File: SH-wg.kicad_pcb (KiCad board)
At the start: 4 copper layers, 55.6 x 79.2 mm, 68 parts, among them J101 Aux PCB Conn Male, J102 Aux PCB Conn Female, J201 Conn_01x05, J501 Conn_01x04, J701 Conn_02x03_Odd_Even, U201 SN65HVD231, U301 ESP32-WROOM-32E, U601 XL1509-3.3, U801 AH1902

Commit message: Add headers & LEDs
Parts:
- added D803: GREEN LED, LED_SMD:LED_0603_1608Metric, F.Cu at (92.2, 97.8)
- added D804: GREEN LED, LED_SMD:LED_0603_1608Metric, F.Cu at (102.8, 97.8)
- added J301: JTAG, Connector_IDC:IDC-Header_2x05_P2.54mm_Vertical, F.Cu at (99.8, 88.6)
- added J302: Digital IO, Connector_PinHeader_2.54mm:PinHeader_1x05_P2.54mm_Vertical, F.Cu at (94.7, 62.0)
- added J303: Analog IO, Connector_PinHeader_2.54mm:PinHeader_1x05_P2.54mm_Vertical, F.Cu at (64.3, 88.6)
- added J401: Power, Connector_PinHeader_2.54mm:PinHeader_2x03_P2.54mm_Vertical, F.Cu at (79.5, 88.6)
- added Q801: 2N7002, Package_TO_SOT_SMD:SOT-23, F.Cu at (62.2, 64.8)
- added R803: 2.2k, Resistor_SMD:R_0402_1005Metric, F.Cu at (92.8, 96.2)
- added R804: 2.2k, Resistor_SMD:R_0402_1005Metric, F.Cu at (102.2, 96.2)
- added R805: 10k, Resistor_SMD:R_0402_1005Metric, F.Cu at (65.5, 65.8)
- moved D802 40.9 mm to (96.2, 58.5)
- moved R802 38.9 mm to (93.5, 58.2), turned to 0 degrees
- moved U801 7.08 mm to (80.5, 97.5)
- moved C801 7.08 mm to (82.5, 97.8)
- moved D805 0.95 mm to (61.1, 61.1)
- moved R806 0.95 mm to (62.8, 60.8)
- renumbered D803 to D805, R803 to R806
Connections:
- D805 pad 1: GND -> Net-(D805-Pad1)
- J101 pad 10: /CAN_TX -> /RXD
- J101 pad 3: /EN -> /IO0
- J101 pad 4: /SCL -> /CAN_TX
- J101 pad 5: /IO0 -> /EN
- J101 pad 6: /SDA -> /CAN_RX
- J101 pad 7: /TXD -> /SCL
- J101 pad 8: /CAN_RX -> /TXD
- J101 pad 9: /RXD -> /SDA
- U301 pad 10: /ESP32/IO25 -> /CAN_RX
- U301 pad 11: /ESP32/IO26 -> /CAN_TX
- U301 pad 12: /ESP32/IO27 -> /CAN_LED_EN
- U301 pad 13: /ESP32/IO14 -> /ESP32/TMS
- U301 pad 14: /ESP32/IO12 -> /ESP32/TDI
- U301 pad 16: /ESP32/IO13 -> /ESP32/TCK
- U301 pad 23: /ESP32/IO15 -> /ESP32/TDO
- U301 pad 29: /ESP32/IO5 -> /RED_LED
- U301 pad 6: /CAN_RX -> /ESP32/IO34
- U301 pad 7: /CAN_TX -> /ESP32/IO35

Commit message: Finish 0.1.0 design
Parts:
- removed C411, C412, C413, C414, C415, C416, C417, C418, C419, C420: 100nF, Capacitor_SMD:C_0402_1005Metric
- added G401: Hat Labs pictogram, SH-wg:HL_pictogram_6.3mm, F.Cu at (70.0, 80.9)
- added G402: Hat Labs logo, SH-wg:Hat_Labs_20mm, B.Cu at (91.1, 129.4)
- added G403: Hat Labs logo large, SH-wg:Hat_Labs_25.4mm, B.Cu at (79.5, 67.1)
- added G404: WEEE logo, Symbol:WEEE-Logo_5.6x8mm_SilkScreen, B.Cu at (79.7, 81.5)
- added G405: OSHW logo, Symbol:OSHW-Logo2_9.8x8mm_SilkScreen, B.Cu at (88.3, 80.8)
- H401: footprint SH-ESP32:MountingSlot_3.2mm_M3_Unplated -> MountingHole:MountingHole_3.2mm_M3
- J302: footprint Connector_PinHeader_2.54mm:PinHeader_1x05_P2.54mm_Vertical -> Connector_PinHeader_2.54mm:PinHeader_1x04_P2.54mm_Vertical
- L602: footprint SH-ESP32:SMMS0650-1R0M -> SH-wg:SMMS0650-1R0M
- R802: value 2k -> 1.5k
- R803, R804: value 2.2k -> 2k
- R806: value 2k -> 2.2k
- U301: footprint SH-ESP32:ESP32-WROOM-32-HandSolder -> SH-wg:ESP32-WROOM-32-HandSolder
- moved C404 63.5 mm to (108.1, 62.1), turned to 90 degrees
- moved C408 60.5 mm to (106.5, 88.0), turned to 0 degrees
- moved C403 57.5 mm to (97.1, 66.6), turned to 0 degrees
- moved C406 53.7 mm to (97.5, 96.2)
- moved C705 52.6 mm to (103.1, 133.8), turned to 90 degrees
- moved C405 51.2 mm to (88.2, 96.2), turned to 0 degrees
- moved C703 49.0 mm to (102.4, 116.5), turned to -90 degrees
- moved C402 45.5 mm to (97.1, 80.6), turned to 180 degrees
- moved C704 45.5 mm to (96.5, 121.6)
- moved C410 25.3 mm to (63.1, 83.8), turned to 180 degrees
- moved C401 24.3 mm to (67.7, 68.8), turned to 0 degrees
- moved C409 24.1 mm to (66.3, 61.8), turned to 90 degrees
- moved C707 21.6 mm to (75.9, 122.5)
- moved C701 20.2 mm to (70.8, 131.3), turned to -90 degrees
- moved C407 19.8 mm to (68.0, 74.2)
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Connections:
- J302 pad 1: /ESP32/IO18 -> /ESP32/IO19
- J302 pad 2: /ESP32/IO19 -> /ESP32/IO21
- J302 pad 3: /ESP32/IO21 -> /ESP32/IO22
- J302 pad 4: /ESP32/IO22 -> /ESP32/IO23
- U301 pad 30: /ESP32/IO18 -> /HALL
- U301 pad 34: /TXD -> /RXD
- U301 pad 35: /RXD -> /TXD
- U801 pad 5: /HALL_OUTPUT -> /HALL
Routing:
- net /CAN_TX: track 0.00 -> 75.4 mm, vias 0 -> 5
- net /CAN_RX: track 0.00 -> 63.6 mm, vias 0 -> 8
- net /CAN_LED_EN: track 0.00 -> 54.5 mm, vias 0 -> 5
- net /SCL: track 0.00 -> 46.8 mm, vias 0 -> 3
- net /ESP32/TMS: track 0.00 -> 44.2 mm, vias 0 -> 2
- net /SDA: track 0.00 -> 44.1 mm, vias 0 -> 3
- net /TXD: track 0.00 -> 40.6 mm, vias 0 -> 2
- net /YELLOW_LED: track 0.00 -> 37.5 mm, vias 0 -> 4
- net /HALL: track 0.00 -> 36.3 mm, vias 0 -> 4
- net /ESP32/TDI: track 0.00 -> 35.7 mm, vias 0 -> 2
- net /ESP32/SENSOR_VP: track 0.00 -> 34.8 mm, vias 0 -> 3
- net /ESP32/TCK: track 0.00 -> 33.6 mm, vias 0 -> 2
- net /ESP32/IO34: track 0.00 -> 33.0 mm, vias 0 -> 3
- net /RXD: track 0.00 -> 31.6 mm, vias 0 -> 2
- net /ESP32/IO32: track 0.00 -> 31.2 mm, vias 0 -> 3
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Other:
- board size 55.6 x 79.2 mm -> 54.6 x 79.2 mm
- board text added: "19"
- board text added: "21"
- board text added: "22"
- board text added: "23"
- board text added: "32"
- board text added: "33"
- board text added: "34"
- board text added: "3V3"
- board text added: "GND"
- board text added: "I2C"
- board text added: "JTAG"
- board text added: "Prog"
- board text added: "SCL"
- board text added: "SDA"
- board text added: "Sailor Hat WiFi Gateway"
- board text added: "VN"
- board text added: "VP"
- board text added: "v0.1.0"
- board text removed: "SH-ESP32"
- board text removed: "Sailor Hat with ESP32"
- board text removed: "https://github.com/hatlabs/SH-ESP32-hardware/"

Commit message: Prepare final 0.1.0 proto
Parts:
- added REF**: Tab, kikit:Tab, F.Cu at (80.8, 83.8)
- added REF**: Tab, kikit:Tab, F.Cu at (42.8, 127.5)
- added REF**: Tab, kikit:Tab, F.Cu at (97.2, 127.6)
- added REF**: Tab, kikit:Tab, F.Cu at (96.5, 44.8)
- added REF**: Tab, kikit:Tab, F.Cu at (70.0, 138.8)
- added REF**: Tab, kikit:Tab, F.Cu at (77.3, 39.1)
- added REF**: Tab, kikit:Tab, F.Cu at (42.2, 57.6)
- added REF**: Tab, kikit:Tab, F.Cu at (70.0, 116.3)
- added REF**: Tab, kikit:Tab, F.Cu at (96.5, 70.5)
- D603: value SS24FL -> DSS34
- L601: value NLCV32T-100K-PFR -> CBC3225T100KR
- U201: value SN65HVD231 -> SN65HVD232DR
- moved C405 24.1 mm to (71.5, 78.8)
- moved C406 24.1 mm to (80.8, 78.8)
- moved R801 24.1 mm to (93.5, 69.5)
- moved U801 24.1 mm to (63.8, 80.1)
- moved C302 24.1 mm to (51.3, 41.7)
- moved C407 24.1 mm to (51.3, 56.8)
- moved D802 24.1 mm to (79.5, 41.1)
- moved G401 24.1 mm to (53.3, 63.5)
- moved H404 24.1 mm to (80.3, 57.6)
- moved J302 24.1 mm to (78.0, 44.6)
- moved Q801 24.1 mm to (45.5, 47.4)
- moved R802 24.1 mm to (76.8, 40.9)
- moved R805 24.1 mm to (48.8, 48.4)
- moved U301 24.1 mm to (63.3, 49.0)
- moved C401 24.1 mm to (51.0, 51.4)
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- renumbered H401 to H404
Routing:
- net GND: vias 78 -> 76
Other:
- board size 54.6 x 79.2 mm -> 54.6 x 99.2 mm
- board text removed: "JLCJLCJLCJLC"

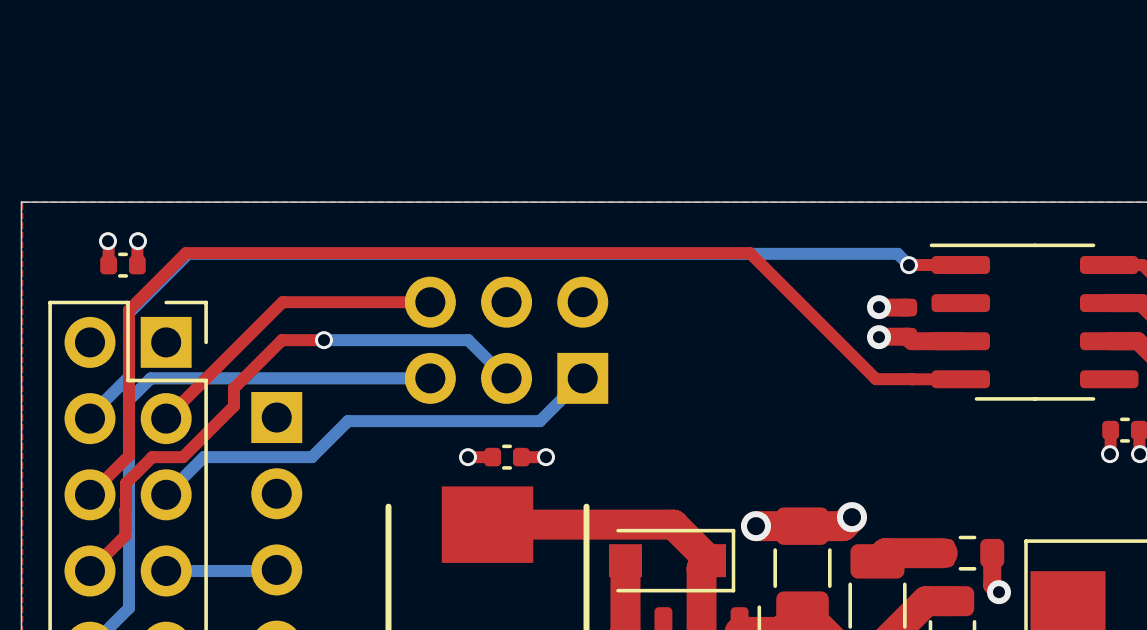
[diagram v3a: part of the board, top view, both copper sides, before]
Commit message: Add a pull-up resistor to CAN TX line
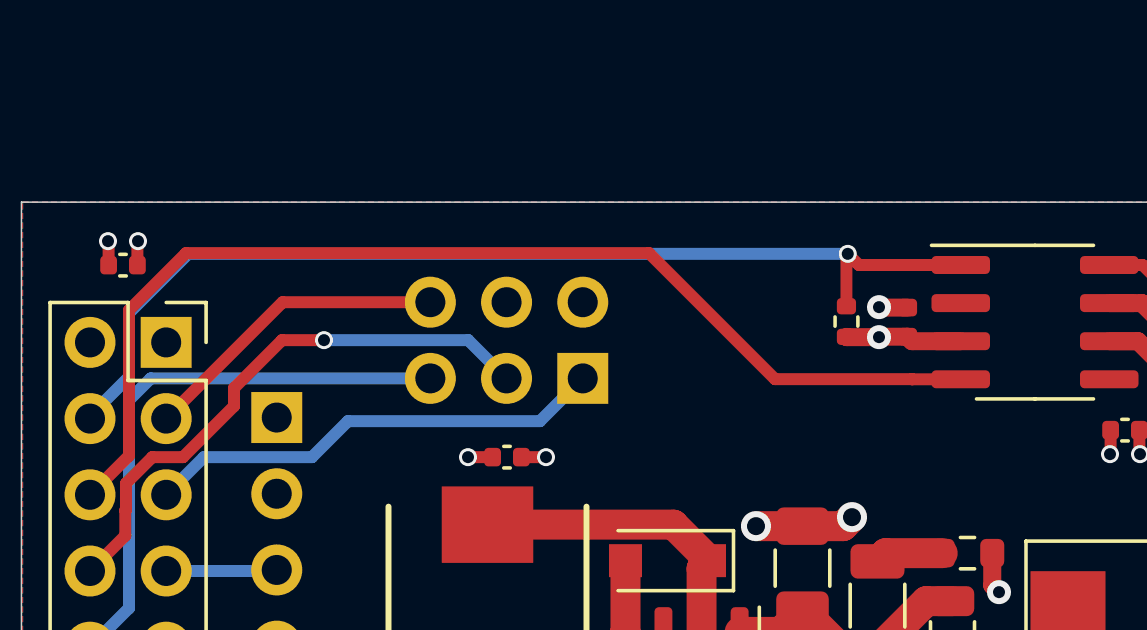
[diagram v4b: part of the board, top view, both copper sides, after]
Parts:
- added R202: 10k, Resistor_SMD:R_0402_1005Metric, F.Cu at (70.5, 120.6)
- D603: value DSS34 -> B5819W
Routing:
- net /CAN_TX_1: track 32.8 -> 34.5 mm
- net +3V3_1: track 20.8 -> 21.9 mm
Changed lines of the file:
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@@
     (descr "D_SOD-123F")
     (tags "D_SOD-123F")
-    (property "LCSC" "C511866")
+    (property "LCSC" "C8598")
     (property "Notes" "")
     (property "Sheetfile" "power-input.kicad_sch")
@@
       (effects (font (size 1 1) (thickness 0.15)))
     )
-    (fp_text value "DSS34" (at 0 2.1) (layer "F.Fab") hide
+    (fp_text value "B5819W" (at 0 2.1) (layer "F.Fab") hide
       (effects (font (size 1 1) (thickness 0.15)))
     )
@@
     (pad "" np_thru_hole circle (at 0 0) (size 3.2 3.2) (drill 3.2) (layers *.Cu *.Mask))
   )
+  (footprint "Resistor_SMD:R_0402_1005Metric" (layer "F.Cu")
+    (at 70.5 120.6 90)
+    (descr "Resistor SMD 0402 (1005 Metric), square (rectangular) end terminal, IPC_7351 nominal, (Body size source: IPC-SM-782 page 72, https://www.pcb-3d.com/wordpress/wp-content/uploads/ipc-sm-782a_amendment_1_and_2.pdf), generated with kicad-footprint-generator")
+    (tags "resistor")
+    (property "LCSC" "C25744")
+    (property "Sheetfile" "canbus.kicad_sch")
+    (property "Sheetname" "CAN bus")
+    (attr smd)
+    (fp_text reference "R202" (at 0 -1.17 90) (layer "F.SilkS") hide
+      (effects (font (size 1 1) (thickness 0.15)))
+    )
+    (fp_text value "10k" (at 0 1.17 90) (layer "F.Fab") hide
+      (effects (font (size 1 1) (thickness 0.15)))
+    )
+    (fp_text user "${REFERENCE}" (at 0 0 90) (layer "F.Fab") hide
+      (effects (font (size 0.26 0.26) (thickness 0.04)))
+    )
+    (fp_line (start -0.153641 0.38) (end 0.153641 0.38) (layer "F.SilkS") (width 0.12))
+    (fp_line (start -0.153641 -0.38) (end 0.153641 -0.38) (layer "F.SilkS") (width 0.12))
+    (fp_line (start 0.93 -0.47) (end 0.93 0.47) (layer "F.CrtYd") (width 0.05))
+    (fp_line (start -0.93 0.47) (end -0.93 -0.47) (layer "F.CrtYd") (width 0.05))
+    (fp_line (start 0.93 0.47) (end -0.93 0.47) (layer "F.CrtYd") (width 0.05))
+    (fp_line (start -0.93 -0.47) (end 0.93 -0.47) (layer "F.CrtYd") (width 0.05))
+    (fp_line (start -0.525 0.27) (end -0.525 -0.27) (layer "F.Fab") (width 0.1))
+    (fp_line (start 0.525 0.27) (end -0.525 0.27) (layer "F.Fab") (width 0.1))
+    (fp_line (start 0.525 -0.27) (end 0.525 0.27) (layer "F.Fab") (width 0.1))
+    (fp_line (start -0.525 -0.27) (end 0.525 -0.27) (layer "F.Fab") (width 0.1))
+    (pad "1" smd roundrect (at -0.51 0 90) (size 0.54 0.64) (layers "F.Cu" "F.Paste" "F.Mask") (roundrect_rratio 0.25)
+      (net 54 "+3V3_1") (pintype "passive"))
+    (pad "2" smd roundrect (at 0.51 0 90) (size 0.54 0.64) (layers "F.Cu" "F.Paste" "F.Mask") (roundrect_rratio 0.25)
+      (net 50 "/CAN_TX_1") (pintype "passive"))
+    (model "${KICAD6_3DMODEL_DIR}/Resistor_SMD.3dshapes/R_0402_1005Metric.wrl"
+      (offset (xyz 0 0 0))
+      (scale (xyz 1 1 1))
+      (rotate (xyz 0 0 0))
+    )
+  )
   (footprint "Capacitor_SMD:C_0402_1005Metric" (layer "F.Cu")
     (at 80.785 78.82)
@@
   (segment (start 45.285 61.43) (end 46.648489 60.066511) (width 0.261112) (layer "B.Cu") (net 49))
   (segment (start 52.338489 60.066511) (end 52.485 59.92) (width 0.261112) (layer "B.Cu") (net 49))
-  (segment (start 74.31 118.715) (end 72.59 118.715) (width 0.4) (layer "F.Cu") (net 50))
-  (segment (start 72.59 118.715) (end 72.585 118.72) (width 0.4) (layer "F.Cu") (net 50))
-  (via (at 72.585 118.72) (size 0.6) (drill 0.4) (layers "F.Cu" "B.Cu") (net 50))
+  (segment (start 74.31 118.715) (end 70.915 118.715) (width 0.4) (layer "F.Cu") (net 50))
+  (segment (start 70.5 120.09) (end 70.5 118.386978) (width 0.4) (layer "F.Cu") (net 50))
+  (segment (start 70.915 118.715) (end 70.543489 118.343489) (width 0.4) (layer "F.Cu") (net 50))
+  (segment (start 70.5 118.386978) (end 70.543489 118.343489) (width 0.4) (layer "F.Cu") (net 50))
+  (via (at 70.543489 118.343489) (size 0.6) (drill 0.4) (layers "F.Cu" "B.Cu") (net 50))
   (segment (start 46.585 120.32) (end 46.585 122.442874) (width 0.4) (layer "B.Cu") (net 50))
   (segment (start 46.585 122.442874) (end 45.285 123.742874) (width 0.4) (layer "B.Cu") (net 50))
-  (segment (start 72.585 118.72) (end 72.208489 118.343489) (width 0.4) (layer "B.Cu") (net 50))
+  (segment (start 70.543489 118.343489) (end 48.561511 118.343489) (width 0.4) (layer "B.Cu") (net 50))
   (segment (start 48.561511 118.343489) (end 46.585 120.32) (width 0.4) (layer "B.Cu") (net 50))
-  (segment (start 72.208489 118.343489) (end 48.561511 118.343489) (width 0.4) (layer "B.Cu") (net 50))
   (segment (start 45.285 123.742874) (end 45.285 123.835) (width 0.4) (layer "B.Cu") (net 50))
-  (segment (start 46.585 120.22) (end 46.585 125.075) (width 0.4) (layer "F.Cu") (net 51))
-  (segment (start 71.485 122.52) (end 67.285 118.32) (width 0.4) (layer "F.Cu") (net 51))
-  (segment (start 72.685 122.52) (end 71.485 122.52) (width 0.4) (layer "F.Cu") (net 51))
-  (segment (start 67.285 118.32) (end 48.485 118.32) (width 0.4) (layer "F.Cu") (net 51))
-  (segment (start 72.69 122.525) (end 72.685 122.52) (width 0.4) (layer "F.Cu") (net 51))
+  (segment (start 72.685 122.52) (end 68.12 122.52) (width 0.4) (layer "F.Cu") (net 51))
+  (segment (start 46.585 125.075) (end 45.285 126.375) (width 0.4) (layer "F.Cu") (net 51))
+  (segment (start 63.92 118.32) (end 48.485 118.32) (width 0.4) (layer "F.Cu") (net 51))
   (segment (start 74.31 122.525) (end 72.69 122.525) (width 0.4) (layer "F.Cu") (net 51))
   (segment (start 48.485 118.32) (end 46.585 120.22) (width 0.4) (layer "F.Cu") (net 51))
-  (segment (start 46.585 125.075) (end 45.285 126.375) (width 0.4) (layer "F.Cu") (net 51))
+  (segment (start 68.12 122.52) (end 63.92 118.32) (width 0.4) (layer "F.Cu") (net 51))
+  (segment (start 46.585 120.22) (end 46.585 125.075) (width 0.4) (layer "F.Cu") (net 51))
+  (segment (start 72.69 122.525) (end 72.685 122.52) (width 0.4) (layer "F.Cu") (net 51))
   (segment (start 47.86 131.42) (end 47.825 131.455) (width 0.4) (layer "B.Cu") (net 52))
   (segment (start 51.51 131.42) (end 47.86 131.42) (width 0.4) (layer "B.Cu") (net 52))
@@
   (segment (start 71.6 121.105) (end 71.585 121.12) (width 0.6) (layer "F.Cu") (net 54))
   (segment (start 64.4 132.235) (end 64.485 132.32) (width 0.4) (layer "F.Cu") (net 54))
+  (segment (start 71.585 121.12) (end 70.51 121.12) (width 0.6) (layer "F.Cu") (net 54))
   (segment (start 85.685 119.6) (end 86.465 119.6) (width 0.4) (layer "F.Cu") (net 54))
   (segment (start 86.385 135.94) (end 87.165 135.94) (width 0.4) (layer "F.Cu") (net 54))
   (segment (start 80.265 125) (end 80.285 125.02) (width 0.4) (layer "F.Cu") (net 54))
   (segment (start 47.065 137.3) (end 47.085 137.32) (width 0.4) (layer "F.Cu") (net 54))
+  (segment (start 70.51 121.12) (end 70.5 121.11) (width 0.6) (layer "F.Cu") (net 54))
   (segment (start 58.335 133.47) (end 58.535 133.27) (width 1) (layer "F.Cu") (net 54))
   (segment (start 57.335 136.07) (end 56.785 136.62) (width 1) (layer "F.Cu") (net 54))
